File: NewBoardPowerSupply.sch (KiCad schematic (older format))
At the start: 12 parts, among them IC1 ADM7172ACPZ-4.2-R7

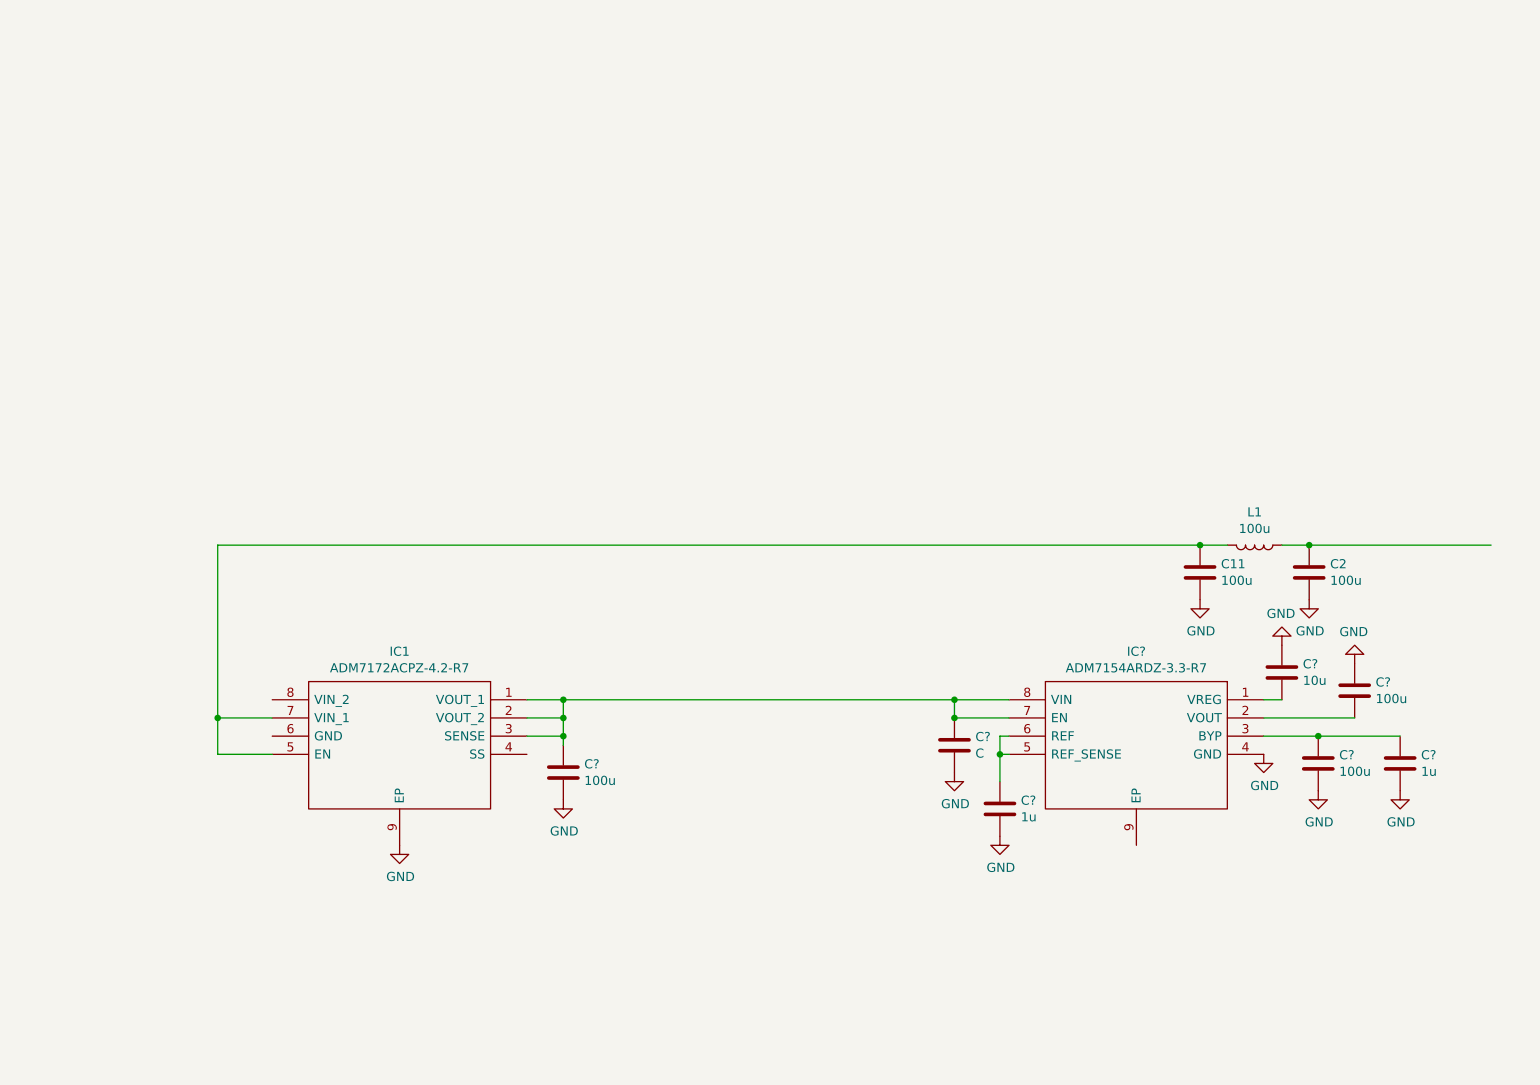
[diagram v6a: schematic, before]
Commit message: added newBoardPowerSupply to the folder
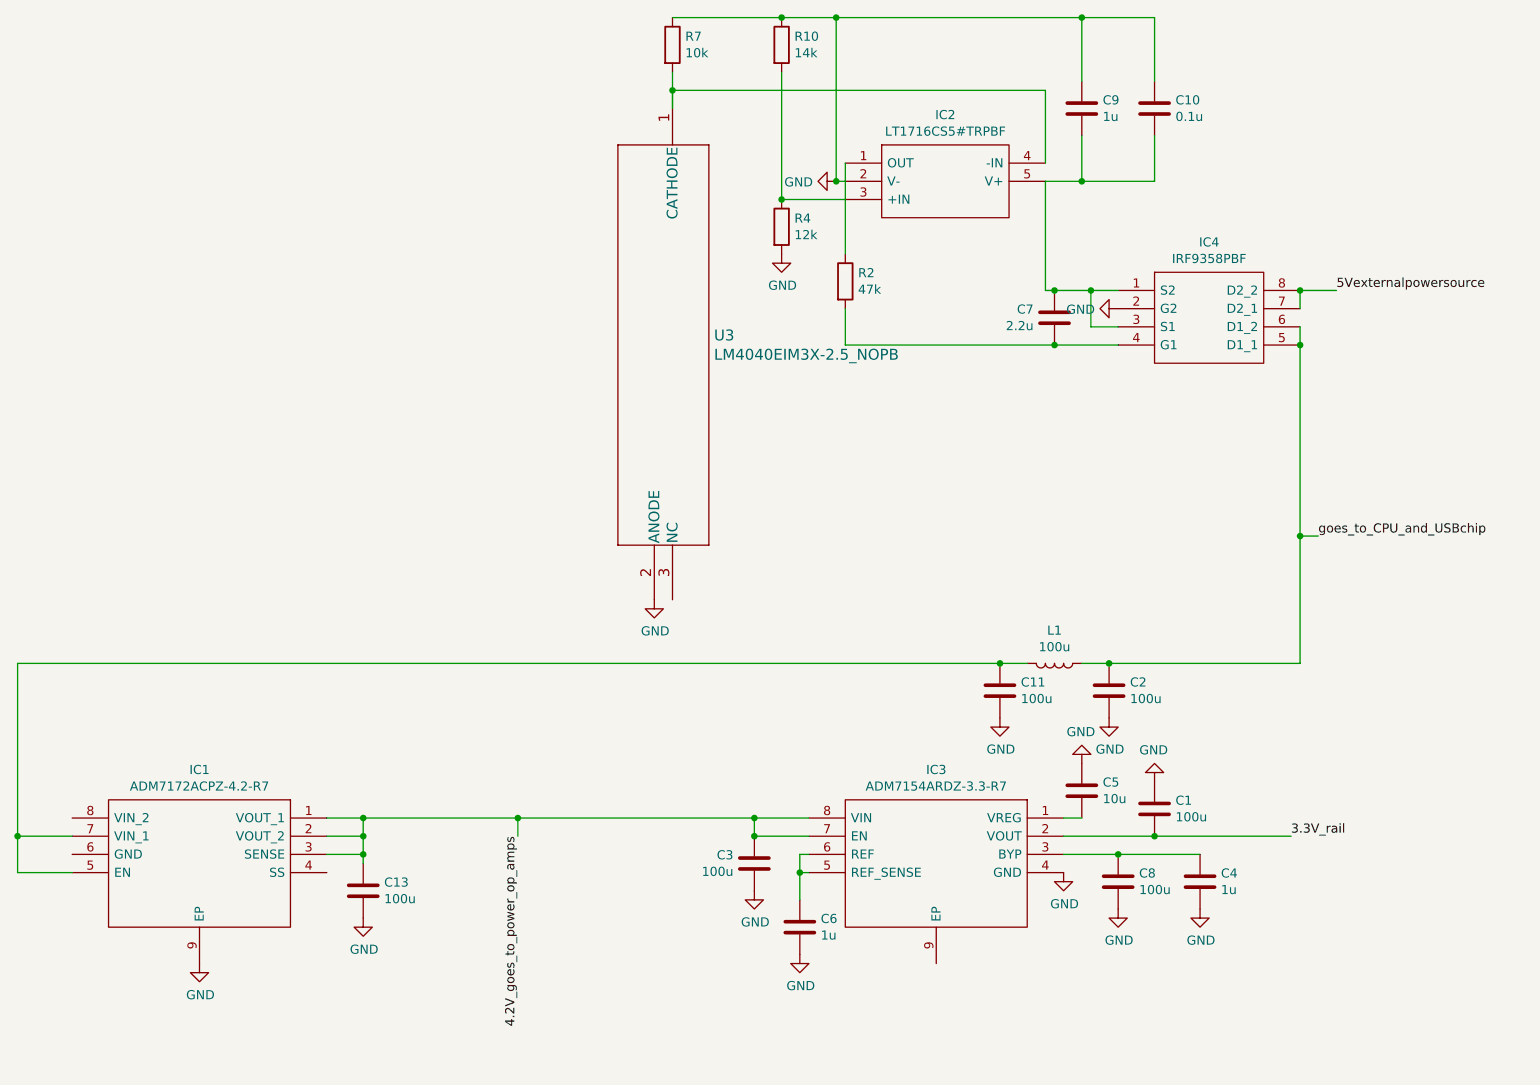
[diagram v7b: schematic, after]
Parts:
- added C10: 0.1u, symbol Device:C
- added C7: 2.2u, symbol Device:C
- added C9: 1u, symbol Device:C
- added IC2: LT1716CS5#TRPBF, SOT95P280X100-5N, symbol LT1716CS5#TRPBF:LT1716CS5#TRPBF
- added IC4: IRF9358PBF, SOIC127P600X175-8N, symbol IRF9358PBF:IRF9358PBF
- added R10: 14k, symbol Device:R
- added R2: 47k, symbol Device:R
- added R4: 12k, symbol Device:R
- added R7: 10k, symbol Device:R
- added U3: LM4040EIM3X-2.5_NOPB, DBZ3, symbol LM4040:LM4040EIM3X-2.5_NOPB
- C3: renamed from C?; value C -> 100u
- gave numbers to parts that had none: 7
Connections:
- net labels added: 3.3V_rail, 4.2V_goes_to_power_op_amps, 5Vexternalpowersource, goes_to_CPU_and_USBchip
- wire segments 26 -> 63
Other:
- moved on the sheet: C1, C11, C13, C2, C3, C4, C5, C6, C8, IC1, IC3, L1

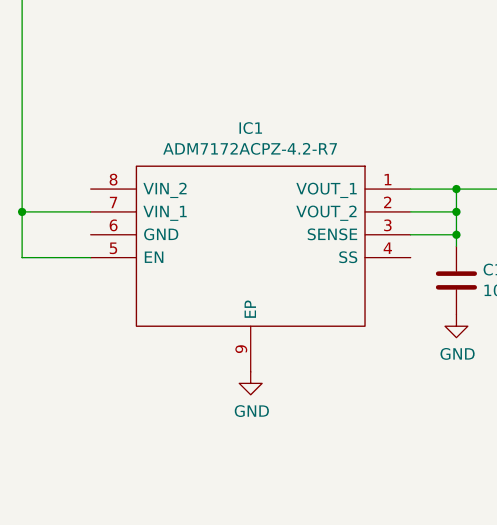
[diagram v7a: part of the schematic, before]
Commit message: grounded GND pin on 4.2V regulator
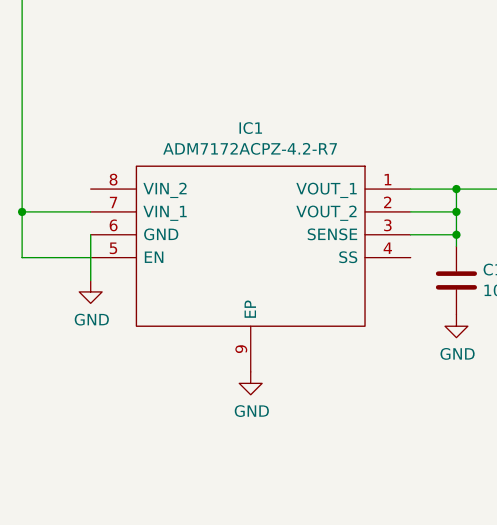
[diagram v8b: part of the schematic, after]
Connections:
- net GND: now also IC1.6 (GND)
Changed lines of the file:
@@
-$EndComp
-$Comp
-L Device:C C2
-U 1 1 60C41D63
-P 7900 4700
-F 0 "C2" H 7785 4654 50  0000 R CNN
-F 1 "100u" H 7785 4745 50  0000 R CNN
-F 2 "" H 7938 4550 50  0001 C CNN
-F 3 "~" H 7900 4700 50  0001 C CNN
-	1    7900 4700
-	-1   0    0    1
 $EndComp
 $Comp
@@
 Wire Wire Line
 	6450 1800 6450 2300
+$Comp
+L Device:C C2
+U 1 1 60C41D63
+P 7900 4700
+F 0 "C2" H 7785 4654 50  0000 R CNN
+F 1 "100u" H 7785 4745 50  0000 R CNN
+F 2 "" H 7938 4550 50  0001 C CNN
+F 3 "~" H 7900 4700 50  0001 C CNN
+	1    7900 4700
+	-1   0    0    1
+$EndComp
+$Comp
+L power:GND #PWR?
+U 1 1 60C8805A
+P 2200 5800
+F 0 "#PWR?" H 2200 5550 50  0001 C CNN
+F 1 "GND" H 2205 5627 50  0000 C CNN
+F 2 "" H 2200 5800 50  0001 C CNN
+F 3 "" H 2200 5800 50  0001 C CNN
+	1    2200 5800
+	1    0    0    -1
+$EndComp
+Wire Wire Line
+	2200 5600 2200 5800
 $EndSCHEMATC
